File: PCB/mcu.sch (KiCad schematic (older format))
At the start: 58 parts, among them J1 DBG, P1 PC, P2 Link, P3 SSD1107, Q1 SSP6206, U1 USBLC6-2SC6, U2 USBLC6-2SC6, U3 STM32F103CBTx

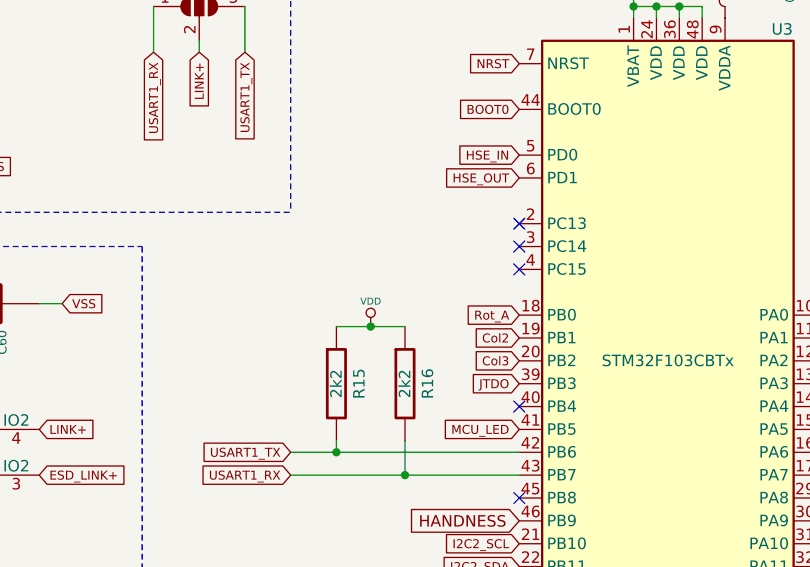
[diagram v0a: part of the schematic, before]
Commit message: Add notes about pull-up resistors
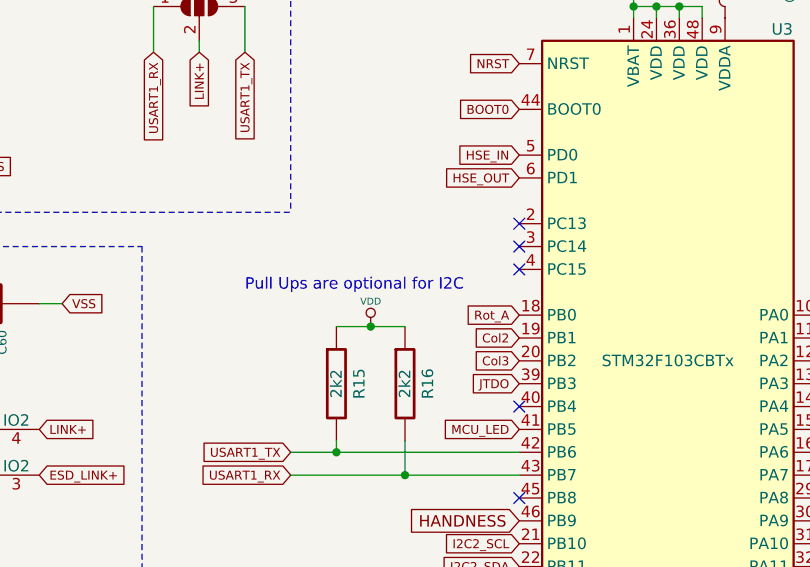
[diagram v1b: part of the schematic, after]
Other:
- note added: "Pull Ups are optional for I2C"
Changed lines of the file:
@@
 Text Notes 550  6150 0    50   ~ 0
 VBUS Filter according to:\nhttp://www.ftdichip.com/Support/Documents/AppNotes/AN_146_USB_Hardware_Design_Guidelines_for_FTDI_ICs.pdf
+Text Notes 4800 3050 0    50   ~ 0
+Pull Ups are optional for I2C
 $EndSCHEMATC

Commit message: Add WIP yaemk 1.2 files
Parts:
- removed C3, C38, C50, C52: 100n, prettylib:SMD-0603, symbol YAEMK:C
- removed R14: 1k5, prettylib:SMD-0603, symbol YAEMK:R
- removed R15, R16: 2k2, prettylib:SMD-0603, symbol YAEMK:R
- removed R8: 33, prettylib:SMD-0603, symbol YAEMK:R
- HSE1: value 12MHz -> 8MHz
- R7: value 33 -> 1k5
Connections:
- net labels added: I2C1_SCL, I2C1_SDA, SPI2_MOSI, SPI2_SCK, USART3_RX, USART3_TX
- net labels removed: I2C2_SCL, I2C2_SDA, TIM2_CH3, USART1_RX, USART1_TX
- wire segments 174 -> 150
- no-connect marks 14 -> 10
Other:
- note removed: "Pull Ups are optional for I2C"

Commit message: Update YAEMK
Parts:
- removed C39: 100n, prettylib:SMD-0603, symbol YAEMK:C
- removed D78: LED, prettylib:LED-0603, symbol YAEMK:LED
- added C3, C38: 100n, prettylib:SMD-0603, symbol YAEMK:C
- added D38, D39: DIODE, Diode_SMD:D_0603_1608Metric, symbol YAEMK:DIODE
- added Q2: Q_PNP_BCE, prettylib:SOT-23, symbol Device:Q_PNP_BCE
- added R14: 1k5, prettylib:SMD-0603, symbol YAEMK:R
- added R15, R16: 33, prettylib:SMD-0603, symbol YAEMK:R
- added R8: 120R, prettylib:SMD-0603, symbol YAEMK:R
- added S7: DFU, prettylib:SMD_Tacticle_Switch_TS24CA, symbol YAEMK:SW
- added U4: 24LC64, Package_SO:TSSOP-8_4.4x3mm_P0.65mm, symbol Memory_EEPROM:24LC64
- JP10, JP3, JP4, JP5, JP6, JP7, JP8, JP9: symbol YAEMK:SolderJumper_2_Open -> YAEMK-rescue:SolderJumper_2_Open-YAEMK
- Q1: symbol YAEMK:SSP6206 -> YAEMK-rescue:SSP6206-YAEMK
- R10: value 10k -> 1M
- R9: value 2k2 -> 1k5
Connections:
- net labels added: BOOT0_CHARGE
- net labels removed: MCU_LED
- wire segments 150 -> 181
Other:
- note added: "I2C EEPROM"
- note added: "Reset and DFU Bootloader Circuit"
- note removed: "Boot Mode"
- note removed: "Reset Button\n"
- moved on the sheet: C37, C42, C43, C44, C45, C46, C47, C48, C49, C56, C57, C59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

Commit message: Update YAEMK 1
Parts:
- removed L2: 600Ω @ 100MHz 1A, prettylib:SMD-0603, symbol YAEMK:L
- HSE1: footprint prettylib:Crystal_SMD_EuroQuartz_MJ-4Pin_5.0x3.2mm -> Crystal:Crystal_SMD_3225-4Pin_3.2x2.5mm
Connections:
- net VDD: now also U3.9 (VDDA)
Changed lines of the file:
@@
 L YAEMK:VDD #PWR025
 U 1 1 5EA004DE
-P 8550 4450
-F 0 "#PWR025" H 8550 4550 30  0001 C CNN
-F 1 "VDD" H 8550 4560 30  0000 C CNN
-F 2 "" H 8550 4450 60  0000 C CNN
-F 3 "" H 8550 4450 60  0000 C CNN
-	1    8550 4450
+P 8550 4700
+F 0 "#PWR025" H 8550 4800 30  0001 C CNN
+F 1 "VDD" H 8550 4810 30  0000 C CNN
+F 2 "" H 8550 4700 60  0000 C CNN
+F 3 "" H 8550 4700 60  0000 C CNN
+	1    8550 4700
 	1    0    0    -1
 $EndComp
@@
 Wire Wire Line
 	8750 4800 8850 4800
-Wire Wire Line
-	8550 4450 8550 4500
 Wire Wire Line
 	8550 8000 8550 7900
@@
 F 0 "HSE1" H 14050 1300 50  0000 L CNN
 F 1 "8MHz" H 14050 1200 50  0000 L CNN
-F 2 "prettylib:Crystal_SMD_EuroQuartz_MJ-4Pin_5.0x3.2mm" H 14400 1050 50  0001 C CNN
+F 2 "Crystal:Crystal_SMD_3225-4Pin_3.2x2.5mm" H 14400 1050 50  0001 C CNN
 F 3 "~" H 14400 1050 50  0001 C CNN
 	1    14400 1050
@@
 	8650 4800 8750 4800
 $Comp
-L YAEMK:L L2
-U 1 1 5F849BB2
-P 8950 4700
-F 0 "L2" H 8907 4654 50  0000 R CNN
-F 1 "600Ω @ 100MHz 1A" H 8907 4745 50  0000 R CNN
-F 2 "prettylib:SMD-0603" H 8950 4700 50  0001 C CNN
-F 3 "~" H 8950 4700 50  0001 C CNN
-	1    8950 4700
-	-1   0    0    1
-$EndComp
-$Comp
 L YAEMK:VSS #PWR026
 U 1 1 5EAADE05
@@
 	1    0    0    -1
 $EndComp
-Wire Wire Line
-	8950 4550 8950 4500
-Wire Wire Line
-	8950 4500 8550 4500
-Connection ~ 8550 4500
-Wire Wire Line
-	8550 4500 8550 4800
 $Comp
 L YAEMK:USB_C_Receptacle_USB2.0 P1
@@
 Wire Wire Line
 	10350 7350 10150 7350
+Wire Wire Line
+	8550 4700 8550 4800
+Wire Wire Line
+	8950 4850 8950 4800
+Wire Wire Line
+	8950 4800 8850 4800
+Connection ~ 8850 4800
 $EndSCHEMATC

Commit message: Sync
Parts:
- removed C44: 10n, prettylib:SMD-0603, symbol YAEMK:C
- removed C46: 100n, prettylib:SMD-0603, symbol YAEMK:C
- removed C48, C56: 100u, prettylib:CP_EIA-3528-12_Kemet-T_Pad1.50x2.35mm_HandSolder, symbol YAEMK:CT
- removed L1: 600R @ 100MHz 1A, prettylib:SMD-0603, symbol YAEMK:L
- removed Q1: SSP6206, prettylib:SOT-23, symbol YAEMK-rescue:SSP6206-YAEMK
- added C39: 10u, prettylib:SMD-0805, symbol YAEMK:C
- added L1: L_Core_Ferrite, Inductor_SMD:L_Taiyo-Yuden_MD-3030, symbol Device:L_Core_Ferrite
- added R20, R21: 1k5, prettylib:SMD-0603, symbol YAEMK:R
- added U5: TLV62568DBV, Package_TO_SOT_SMD:SOT-23-5, symbol Regulator_Switching:TLV62568DBV
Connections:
- net USB_VBUS: now also C37.1, U5.1 (EN), U5.4 (VIN)
- net VDD: now also C39.1, L1.2, R20.1; no longer C37.1
- net VSS: now also C39.2, R21.2, U5.2 (GND)
- new net: L1.1, U5.3 (SW)
- new net: R20.2, R21.1, U5.5 (FB)
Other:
- note removed: "USB VBUS Filter"
- note removed: "VBUS Filter according to:\nhttp://www.ftdichip.com/Support/Documents/AppNotes/AN_146_USB_Hardware_Design_Guidelines_for_FTDI_ICs.pdf"
- moved on the sheet: D77, R6

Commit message: One step further
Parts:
- removed JP10, JP3, JP4, JP5, JP6, JP7, JP8, JP9: SolderJumper_2_Open, prettylib:SOLDER_JUMPER_2, symbol YAEMK-rescue:SolderJumper_2_Open-YAEMK
- removed JP11: HANDNESS, prettylib:SOLDER_JUMPER_3, symbol YAEMK:SolderJumper_3_Open
- added D77: D_Schottky, Diode_SMD:D_SOD-123F, symbol Device:D_Schottky
- added R22, R23, R24, R25: 1k5, prettylib:SMD-0603, symbol YAEMK:R
- D68: renamed from D38; footprint Diode_SMD:D_0603_1608Metric -> Diode_SMD:D_SOD-523
- D69: renamed from D39; footprint Diode_SMD:D_0603_1608Metric -> Diode_SMD:D_SOD-523
- renumbered C42 to C36, C43 to C37, C45 to C38, C47 to C39, C3 to C40, C49 to C41, C38 to C42, C37 to C43, C39 to C44, C60 to C45, C57 to C46, C59 to C47, D77 to D70, Q2 to Q1, R4 to R10, R8 to R11, R3 to R12, R2 to R13, R10 to R14, R20 to R15, R21 to R16, R6 to R17, R15 to R18, R16 to R19, R7 to R20, R13 to R21, R1 to R5, R11 to R6, R9 to R7, R14 to R8, R5 to R9, S7 to S32, S6 to S33, U4 to U1, U5 to U2, U1 to U3, U2 to U4, U3 to U5
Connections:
- net Col2: now also U5.14 (PA4); no longer U5.19 (PB1)
- net HANDNESS: now also U5.2 (PC13), R24.2, R25.1; no longer U5.41 (PB5)
- net I2C1_SCL: now also P3.2 (P2)
- net I2C1_SDA: now also P3.1 (P1)
- net Row1: no longer U5.31 (PA10)
- net Row4: no longer U5.14 (PA4)
- net USB_VBUS: now also D77.2 (A), R22.1; no longer C43.1, C45.2, P2.A4 (VBUS), P2.A9 (VBUS), P2.B4 (VBUS), P2.B9 (VBUS), U2.1 (EN), U2.4 (VIN), U4.5 (VBUS)
- net VDD: now also P3.3 (P3), R24.1
- net VSS: now also P3.4 (P4), R23.2, R25.2
- net TIM2_CH3: now reaches U5.12 (PA2)
- net SPI2_MOSI: no longer names the net of U5.28 (PB15)
- net SPI2_SCK: no longer names the net of U5.26 (PB13)
- new net SPLIT_DETECT: R22.2, R23.1, U5.31 (PA10)
- new net USB_VBUS_IN: C43.1, C45.2, D77.1 (K), P2.A4 (VBUS), P2.A9 (VBUS), P2.B4 (VBUS), P2.B9 (VBUS), U2.1 (EN), U2.4 (VIN), U4.5 (VBUS)
- no-connect marks 10 -> 9
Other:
- moved on the sheet: C43, C44, D70, L1, R15, R16, R17, U2

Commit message: RC
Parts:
- U5: value STM32F103CBTx -> STM32F303CCTx; symbol YAEMK:STM32F103CBTx -> MCU_ST_STM32F3:STM32F303CCTx
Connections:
- net Col1: now also U5.12 (PA2); no longer U5.13 (PA3)
- net Col2: now also U5.17 (PA7); no longer U5.14 (PA4)
- net Col3: now also U5.18 (PB0); no longer U5.20 (PB2)
- net Col4: now also U5.19 (PB1); no longer U5.25 (PB12)
- net Col5: now also U5.20 (PB2)
- net Col6: now also U5.26 (PB13); no longer U5.30 (PA9)
- net Col7: now also U5.27 (PB14)
- net Col8: now also U5.28 (PB15); no longer U5.29 (PA8)
- net Rot_A: now also U5.13 (PA3); no longer U5.18 (PB0)
- net Rot_B: now also U5.14 (PA4); no longer U5.17 (PA7)
- net Row1: now also U5.29 (PA8)
- net Row2: now also U5.25 (PB12); no longer U5.27 (PB14)
- net Row4: now also U5.15 (PA5)
- net Row5: now also U5.11 (PA1); no longer U5.15 (PA5)
- net TIM2_CH3: now also U5.10 (PA0); no longer U5.12 (PA2)
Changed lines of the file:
@@
 Wire Notes Line
 	2450 600  2450 2700
-$Comp
-L YAEMK:STM32F103CBTx U5
-U 1 1 5E921694
-P 8750 6350
-F 0 "U5" H 9200 7800 50  0000 C CNN
-F 1 "STM32F103CBTx" H 8700 6350 50  0000 C CNN
-F 2 "prettylib:LQFP-48_7x7mm_P0.5mm" H 8150 4950 50  0001 R CNN
-F 3 "http://www.st.com/st-web-ui/static/active/en/resource/technical/document/datasheet/CD00161566.pdf" H 8750 6350 50  0001 C CNN
-	1    8750 6350
-	1    0    0    -1
-$EndComp
 Wire Notes Line
 	14900 3850 15900 3850
@@
 Wire Notes Line
 	2450 600  5000 600
-Text GLabel 9350 6550 2    39   Input ~ 0
+Text GLabel 9350 6850 2    39   Input ~ 0
 Col2
+Text GLabel 8050 6150 0    39   Input ~ 0
+Col3
+Text GLabel 9350 6350 2    39   Input ~ 0
+Col1
+Text GLabel 8050 6250 0    39   Input ~ 0
+Col4
 Text GLabel 8050 6350 0    39   Input ~ 0
-Col3
-Text GLabel 9350 6450 2    39   Input ~ 0
-Col1
-Text GLabel 8050 7350 0    39   Input ~ 0
-Col4
-Text GLabel 8000 8400 0    39   Input ~ 0
 Col5
-Text GLabel 9350 7050 2    39   Input ~ 0
+Text GLabel 8050 7450 0    39   Input ~ 0
 Col6
-Text GLabel 8050 8550 0    39   Input ~ 0
+Text GLabel 8050 7550 0    39   Input ~ 0
 Col7
 Text GLabel 9350 6750 2    39   Input ~ 0
 Row3
-Text GLabel 10000 5950 2    39   Input ~ 0
+Text GLabel 9350 6650 2    39   Input ~ 0
 Row4
-Text GLabel 9350 6650 2    39   Input ~ 0
+Text GLabel 9350 6250 2    39   Input ~ 0
 Row5
-Text GLabel 10100 6450 2    39   Input ~ 0
+Text GLabel 9350 6950 2    39   Input ~ 0
 Row1
-Text GLabel 8050 7550 0    39   Input ~ 0
+Text GLabel 8050 7350 0    39   Input ~ 0
 Row2
-Text GLabel 9350 6950 2    39   Input ~ 0
+Text GLabel 8050 7650 0    39   Input ~ 0
 Col8
 NoConn ~ 3600 1100
@@
 Text GLabel 15300 4500 0    39   Input ~ 0
 JTMS
-Text GLabel 8050 6150 0    39   Input ~ 0
+Text GLabel 9350 6450 2    39   Input ~ 0
 Rot_A
-Text GLabel 9350 6850 2    39   Input ~ 0
+Text GLabel 9350 6550 2    39   Input ~ 0
 Rot_B
 Wire Wire Line
@@
 	13050 2000 12250 2000
 Connection ~ 12250 2000
-Text GLabel 9350 6350 2    39   Input ~ 0
+Text GLabel 9350 6150 2    39   Input ~ 0
 TIM2_CH3
 $Comp
@@
 Text GLabel 14950 3250 2    39   Input ~ 0
 HANDNESS
+$Comp
+L MCU_ST_STM32F3:STM32F303CCTx U5
+U 1 1 5E921694
+P 8750 6350
+F 0 "U5" H 9200 7800 50  0000 C CNN
+F 1 "STM32F303CCTx" H 8700 6350 50  0000 C CNN
+F 2 "prettylib:LQFP-48_7x7mm_P0.5mm" H 8150 4950 50  0001 R CNN
+F 3 "http://www.st.com/st-web-ui/static/active/en/resource/technical/document/datasheet/CD00161566.pdf" H 8750 6350 50  0001 C CNN
+	1    8750 6350
+	1    0    0    -1
+$EndComp
 $EndSCHEMATC
